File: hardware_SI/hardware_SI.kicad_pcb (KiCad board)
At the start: 2 copper layers, 228 x 147.6 mm, 58 parts, among them J1 Barrel_Jack_Switch, J2 Conn_01x07_Female, J3 USB_B_Micro, Q1 SI2323DS-T1, Q2 SI2323DS-T1, SW1 SW_SPDT, U1 OMEGA2+, U2 LTC4085EDEPBF, U3 TPS61200DRC, U4 LD1117S33TR_SOT223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

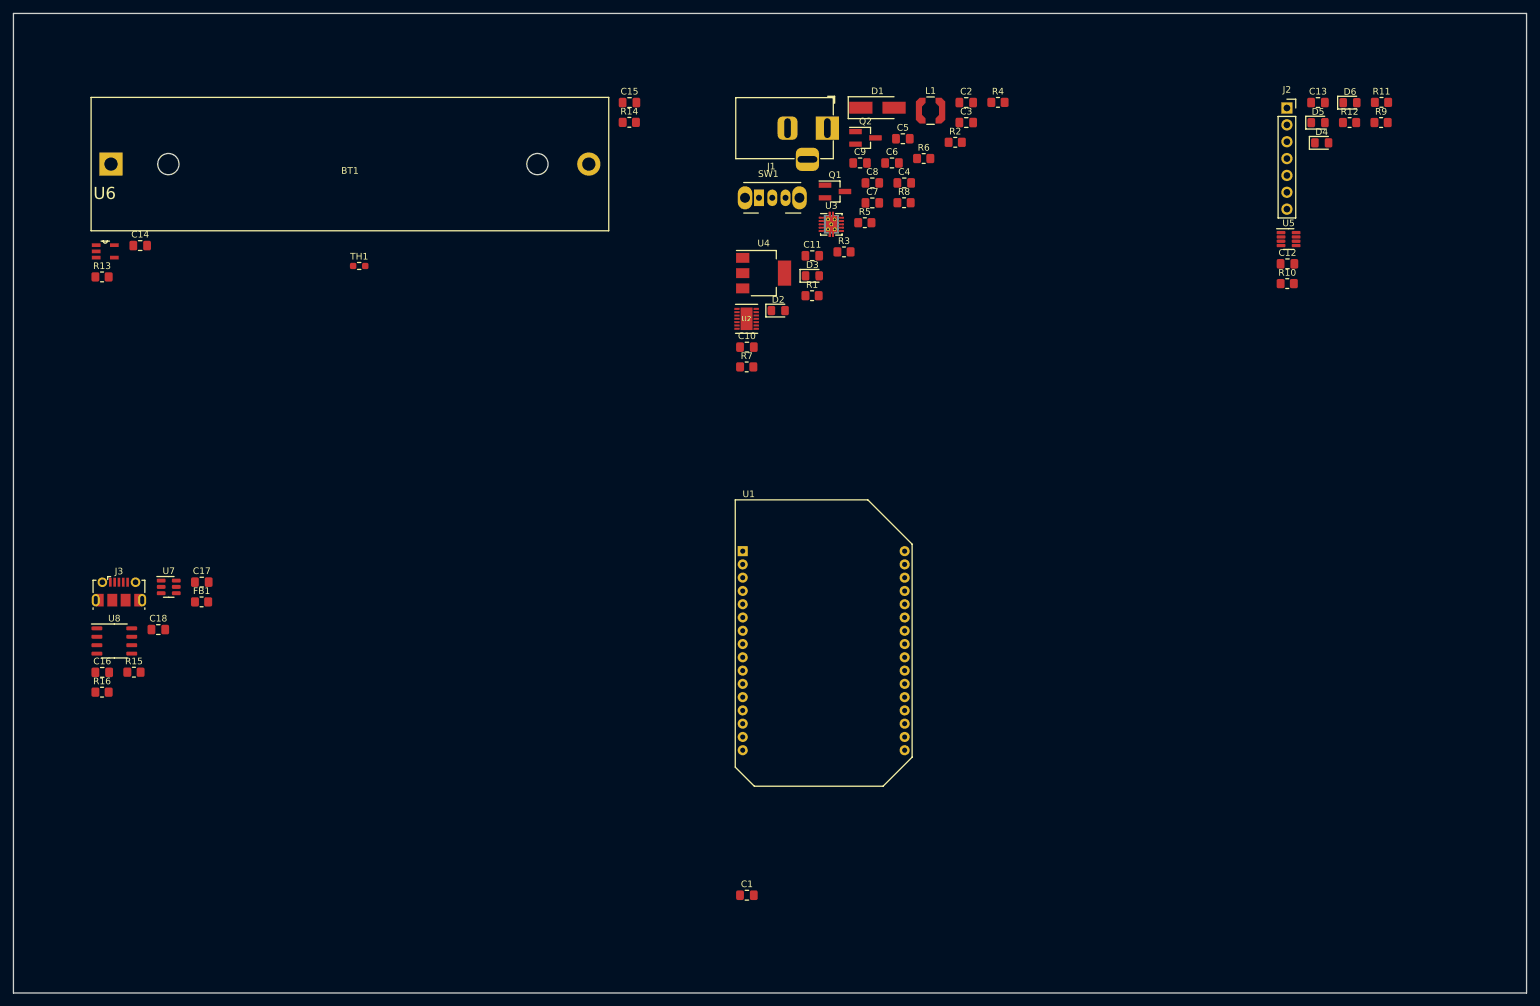
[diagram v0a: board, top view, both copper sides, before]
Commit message: Rutas de PCB
- Se realiza la PCB y se asignan sus respectivas rutas.
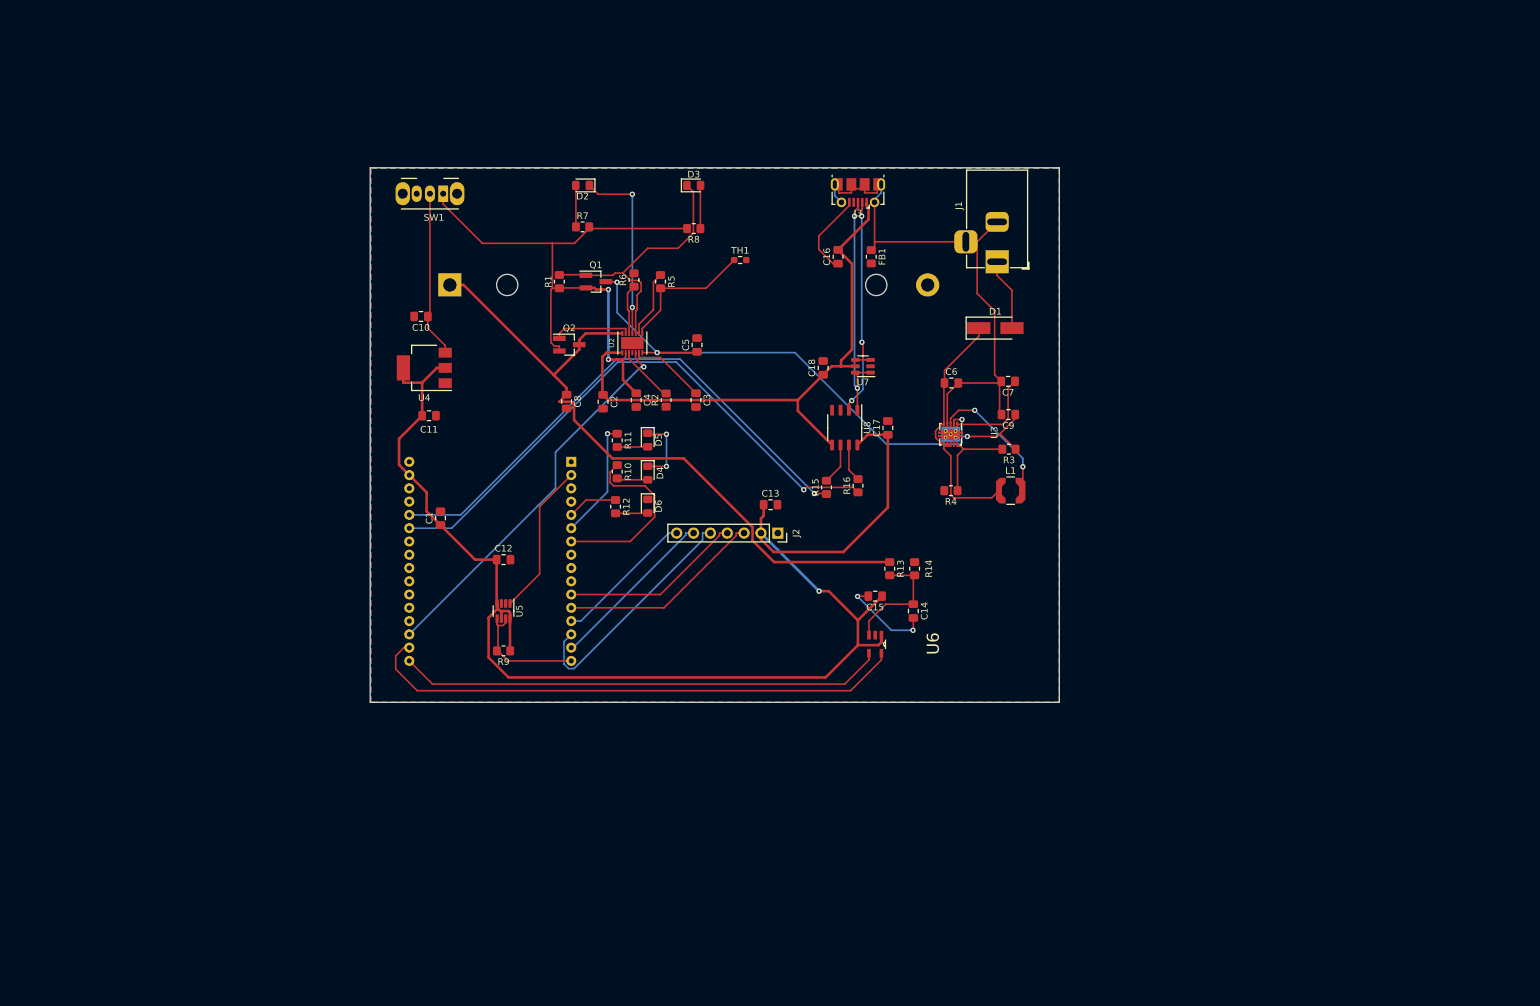
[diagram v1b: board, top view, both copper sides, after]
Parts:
- BT1, U1: moved to B.Cu
- moved R9 154.3 mm to (121.2, 120.2), turned to 180 degrees
- moved U5 130.9 mm to (121.2, 114.2), turned to -90 degrees
- moved U6 130.2 mm to (177.2, 119.2), turned to -90 degrees
- moved C14 128.9 mm to (183.0, 114.2), turned to -90 degrees
- moved C16 127.3 mm to (171.7, 60.9), turned to 90 degrees
- moved J3 126.6 mm to (174.7, 51.2), turned to 180 degrees
- moved R13 126.6 mm to (179.4, 107.9), turned to -90 degrees
- moved C12 126.2 mm to (121.2, 106.5)
- moved R11 125.9 mm to (138.4, 88.5), turned to -90 degrees
- moved R12 124.8 mm to (138.1, 98.5), turned to -90 degrees
- moved D6 122.0 mm to (143.0, 98.5), turned to -90 degrees
- moved R16 118.1 mm to (174.7, 95.4), turned to 90 degrees
- moved U8 114.7 mm to (172.7, 86.6), turned to -90 degrees
- moved FB1 113.5 mm to (176.7, 60.9), turned to -90 degrees
- moved D4 113.1 mm to (143.0, 93.5), turned to -90 degrees
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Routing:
- net +3V3: track 0.00 -> 209.1 mm, vias 0 -> 1
- net +BATT: track 0.00 -> 102.7 mm
- net +5VP: track 0.00 -> 93.4 mm, vias 0 -> 4
- net +5VL: track 0.00 -> 87.6 mm, vias 0 -> 2
- net +5VA: track 0.00 -> 86.7 mm
- net /TX0: track 0.00 -> 86.4 mm, vias 0 -> 1
- net GNDPWR: track 0.00 -> 86.3 mm
- net /SCL: track 0.00 -> 82.0 mm
- net /RX0: track 0.00 -> 81.0 mm, vias 0 -> 1
- net /SDA: track 0.00 -> 73.2 mm
- net /IO19: track 0.00 -> 57.9 mm, vias 0 -> 1
- net /sistema_alimentacion/*ACPR: track 0.00 -> 41.8 mm
- net Net-(C6-Pad1): track 0.00 -> 38.9 mm
- net GND: track 0.00 -> 38.5 mm, vias 0 -> 4
- net Net-(J3-Pad2): track 0.00 -> 37.3 mm, vias 0 -> 3
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- added copper zone on B.Cu, net GND
- added copper zone on F.Cu, net GND
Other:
- board size 228 x 147.6 mm -> 103.8 x 80.5 mm

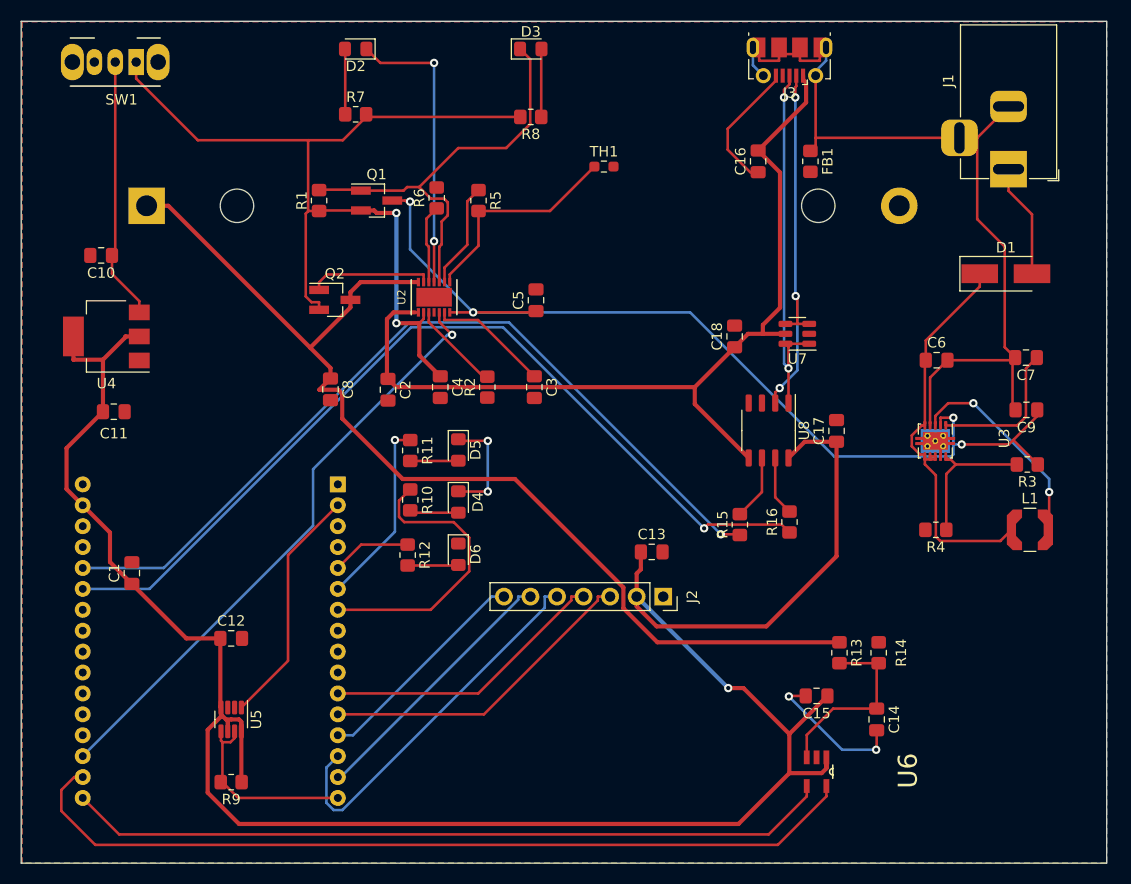
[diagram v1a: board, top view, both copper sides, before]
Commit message: Cambio en alimentación y zona GNDPWR
- Debido a los tiempos de entrega del LTC4085, se cambia el sistema de alimentación, agregando un selector automático de fuente y un integrado de manejo de batería.
- En consecuencia de lo anterior, se usa un LDO con menor voltaje de dropout.
- Se cambia el convertidor DC-DC debido a su alto precio.
- En cuanto a PCB, se completa el circuito del convertidor DC-DC y la zona de GNPWR.
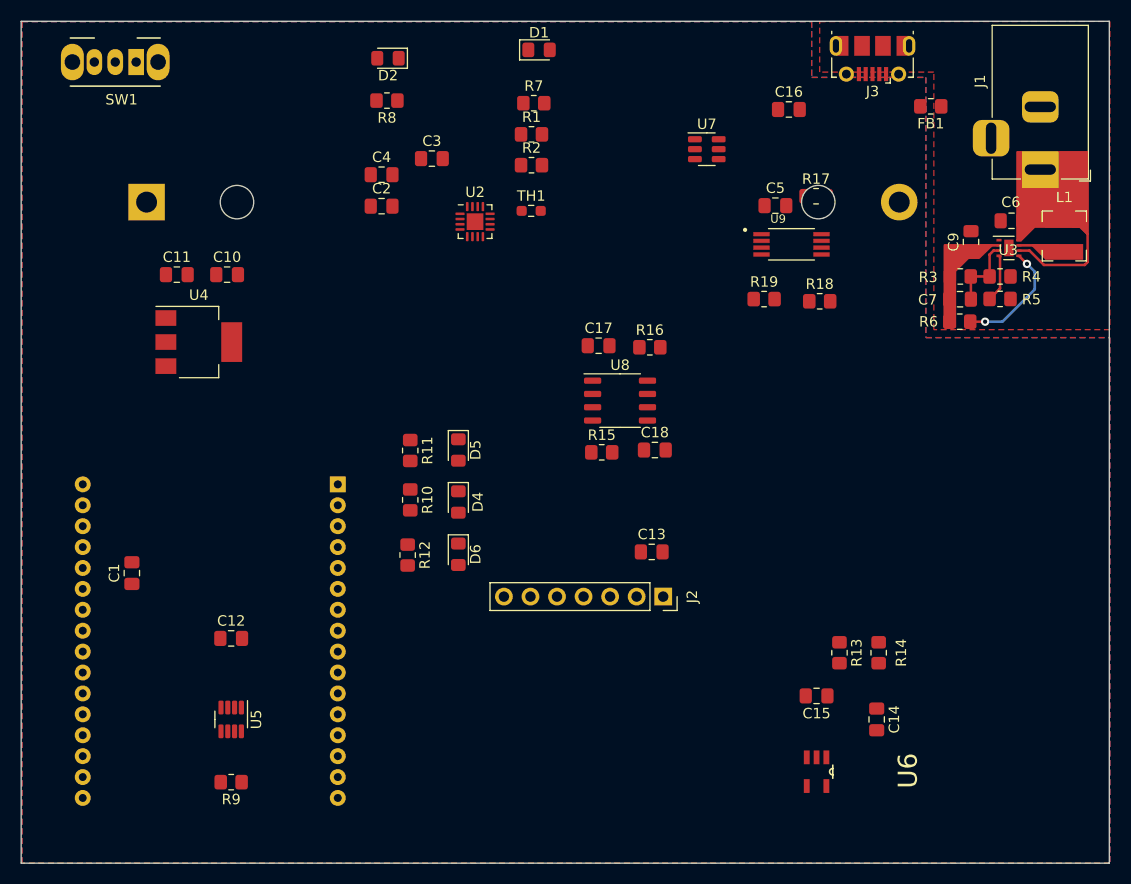
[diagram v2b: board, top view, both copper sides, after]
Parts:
- removed C8: 100n, Capacitor_SMD:C_0805_2012Metric_Pad1.18x1.45mm_HandSolder
- removed D3: WALL_LED, LED_SMD:LED_0805_2012Metric_Pad1.15x1.40mm_HandSolder
- removed Q1, Q2: SI2323DS-T1, Package_TO_SOT_SMD:SOT-23_Handsoldering
- added R17: 10k, Resistor_SMD:R_0805_2012Metric_Pad1.20x1.40mm_HandSolder, F.Cu at (177.2, 64.2)
- added R18: 2.2k, Resistor_SMD:R_0805_2012Metric_Pad1.20x1.40mm_HandSolder, F.Cu at (177.6, 74.2)
- added R19: 400, Resistor_SMD:R_0805_2012Metric_Pad1.20x1.40mm_HandSolder, F.Cu at (172.2, 74.0)
- added U9: TPS2111APWR, TPS2111APWR:SOP65P640X120-8N, F.Cu at (174.8, 68.8)
- C10: value 100n -> 1uF
- C11: value 10u -> 4.7uF
- C2: value 4.7uF -> 1uF
- C3: value 0.1uF -> 4.7uF
- C7: value 100n -> 100pF
- C9: value 10uF -> 22uF
- D1: value 1N4007 -> PGOOD_LED; footprint Diode_SMD:D_SMA_Handsoldering -> LED_SMD:LED_0805_2012Metric_Pad1.15x1.40mm_HandSolder
- L1: value 2.2uH -> 1uH; footprint Inductor_SMD:L_Coilcraft_LPS4018 -> Inductor_SMD:L_Bourns-SRN4018
- R1: value 1k -> 1.5k
- R2: value 2.1k -> 1.5k
- R3: value 1.5M -> 768k
- R4: value 180k -> 243k
- R6: value 10k -> 1M
- R7, R8: value 510 -> 1.5k
- U2: value LTC4085EDEPBF -> BQ24072RGT; footprint LTC4085EDEPBF:DFN-14_DE -> Package_DFN_QFN:VQFN-16-1EP_3x3mm_P0.5mm_EP1.6x1.6mm
- U3: value TPS61200DRC -> TPS61252DSG; footprint Package_SON:Texas_S-PVSON-N10_ThermalVias -> Package_SON:WSON-8-1EP_2x2mm_P0.5mm_EP0.9x1.6mm
- U4: value LD1117S33TR_SOT223 -> LDL1117S33R
- moved R6 51.4 mm to (190.9, 76.2), turned to 180 degrees
- moved R5 50.8 mm to (194.8, 74.0), turned to 0 degrees
- moved D1 49.5 mm to (150.7, 50.2)
- moved L1 28.3 mm to (200.9, 68.0), turned to -90 degrees
- moved R4 25.0 mm to (194.8, 71.9), turned to 0 degrees
- moved C5 24.6 mm to (173.3, 65.1), turned to 0 degrees
- moved C17 24.2 mm to (156.4, 78.5), turned to 0 degrees
- moved C3 24.0 mm to (140.4, 60.6), turned to 0 degrees
- moved R2 21.6 mm to (150.0, 61.2), turned to 0 degrees
- moved R16 21.4 mm to (161.3, 78.7), turned to 0 degrees
- moved R1 21.3 mm to (150.0, 58.3), turned to 0 degrees
- moved C4 21.1 mm to (135.6, 62.1), turned to 0 degrees
- moved U3 19.8 mm to (195.7, 69.2), turned to 0 degrees
- moved U7 19.7 mm to (166.8, 59.7), turned to 0 degrees
- moved R3 19.1 mm to (191.0, 71.9), turned to 0 degrees
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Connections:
- C2 pad 1: +5VA -> GND
- C2 pad 2: GND -> +5VL
- C3 pad 1: Net-(C3-Pad1) -> VCC
- C4 pad 1: +5VL -> +BATT
- C5 pad 1: +5VP -> +5VL
- C6 pad 1: Net-(C6-Pad1) -> Net-(J1-Pad1)
- C7 pad 1: Net-(C7-Pad1) -> +5VP
- C7 pad 2: GNDPWR -> Net-(C7-Pad2)
- D1 pad 1: Net-(C6-Pad1) -> Net-(D1-Pad1)
- J1 pad 1: Net-(D1-Pad2) -> Net-(J1-Pad1)
- L1 pad 1: Net-(C6-Pad1) -> Net-(J1-Pad1)
- R1 pad 1: +5VL -> GND
- R1 pad 2: /sistema_alimentacion/*ACPR -> Net-(R1-Pad2)
- R3 pad 2: Net-(R3-Pad2) -> Net-(C7-Pad2)
- R4 pad 1: Net-(R3-Pad2) -> Net-(C7-Pad2)
- R4 pad 2: GND -> GNDPWR
- R5 pad 2: Net-(R5-Pad2) -> GNDPWR
- R6 pad 2: GND -> +5VP
- R7 pad 1: Net-(D2-Pad2) -> Net-(D1-Pad2)
- R7 pad 2: +5VL -> VCC
- R8 pad 1: Net-(D3-Pad2) -> Net-(D2-Pad2)
- R8 pad 2: +5VL -> VCC
- SW1 pad 1: +5VL -> VCC
- TH1 pad 1: Net-(R5-Pad2) -> Net-(TH1-Pad1)
- U2 pad 1: +5VA -> Net-(TH1-Pad1)
- U2 pad 10: /sistema_alimentacion/*ACPR -> VCC
- U2 pad 11: Net-(D2-Pad1) -> VCC
- U2 pad 12: Net-(R6-Pad1) -> Net-(R1-Pad2)
- U2 pad 13: Net-(Q2-Pad1) -> +5VL
- U2 pad 14: +BATT -> unconnected-(U2-Pad14)
- U2 pad 2: +5VL -> +BATT
- U2 pad 3: Net-(R2-Pad2) -> +BATT
- U2 pad 4: /IO18 -> GND
- U2 pad 5: /IO19 -> VCC
- U2 pad 6: Net-(C3-Pad1) -> GND
- U2 pad 7: +5VP -> Net-(D1-Pad1)
- U2 pad 8: Net-(R5-Pad2) -> GND
- U2 pad 9: Net-(R5-Pad1) -> Net-(D2-Pad1)
- U3 pad 1: Net-(C7-Pad1) -> GNDPWR
- U3 pad 3: Net-(L1-Pad2) -> Net-(C7-Pad2)
- U3 pad 4: GNDPWR -> Net-(R5-Pad1)
- U3 pad 5: Net-(C6-Pad1) -> Net-(R6-Pad1)
- U3 pad 6: Net-(C6-Pad1) -> Net-(J1-Pad1)
- U3 pad 7: Net-(C6-Pad1) -> Net-(L1-Pad2)
- U3 pad 8: Net-(C6-Pad1) -> Net-(J1-Pad1)
- U3 pad 9: GND -> GNDPWR
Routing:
- net +3V3: track 209.1 -> 0.00 mm, vias 1 -> 0
- net +BATT: track 102.7 -> 0.00 mm
- net +5VL: track 87.6 -> 0.00 mm, vias 2 -> 0
- net +5VA: track 86.7 -> 0.00 mm
- net /TX0: track 86.4 -> 0.00 mm, vias 1 -> 0
- net GNDPWR: track 86.3 -> 0.00 mm
- net +5VP: track 93.4 -> 10.4 mm, vias 4 -> 0
- net /SCL: track 82.0 -> 0.00 mm
- net /RX0: track 81.0 -> 0.00 mm, vias 1 -> 0
- net /SDA: track 73.2 -> 0.00 mm
- net /IO19: track 57.9 -> 0.00 mm, vias 1 -> 0
- net /sistema_alimentacion/*ACPR: track 41.8 -> 0.00 mm
- net Net-(C6-Pad1): track 38.9 -> 0.00 mm
- net GND: track 38.5 -> 0.00 mm, vias 4 -> 0
- net Net-(J3-Pad2): track 37.3 -> 0.00 mm, vias 3 -> 0
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- added copper zone on F.Cu, net GNDPWR
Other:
- board size 103.8 x 80.5 mm -> 104.1 x 80.5 mm

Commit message: PCB corregido
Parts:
- added ?: , , F.Cu at (128.8, 50.2)
- added ?: , , F.Cu at (203.8, 122.0)
- added ?: , , F.Cu at (128.8, 121.8)
- moved BT1 90.2 mm to (201.9, 80.7), turned to 180 degrees
- moved C1 61.5 mm to (170.5, 118.6), turned to 180 degrees
- moved R9 51.0 mm to (170.6, 107.2), turned to 0 degrees
- moved C12 49.8 mm to (170.5, 113.8), turned to 180 degrees
- moved U5 49.5 mm to (170.6, 110.5), turned to 90 degrees
- moved U1 38.4 mm to (169.5, 96.6), turned to -90 degrees
- moved SW1 38.3 mm to (150.4, 50.5)
- moved C4 34.5 mm to (170.0, 65.5), turned to 90 degrees
- moved C18 32.7 mm to (169.3, 56.6), turned to -90 degrees
- moved C11 31.2 mm to (147.0, 67.8), turned to 90 degrees
- moved C2 30.0 mm to (165.1, 70.9), turned to 90 degrees
- moved R15 28.5 mm to (158.6, 60.3)
- moved U4 27.1 mm to (142.2, 65.6), turned to -90 degrees
- moved U8 27.0 mm to (165.5, 57.6), turned to 90 degrees
- moved R8 26.9 mm to (162.9, 52.3)
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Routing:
- net +3V3: track 0.00 -> 212.4 mm, vias 0 -> 1
- net /TX0: track 0.00 -> 79.5 mm, vias 0 -> 2
- net /RX0: track 0.00 -> 78.7 mm
- net +BATT: track 0.00 -> 65.5 mm
- net VCC: track 0.00 -> 54.6 mm, vias 0 -> 2
- net /CS1: track 0.00 -> 40.1 mm
- net /D/C: track 0.00 -> 40.0 mm
- net /RST_W: track 0.00 -> 38.6 mm
- net /RST_OLED: track 0.00 -> 35.8 mm
- net +5VA: track 0.00 -> 33.6 mm
- net /IO15: track 0.00 -> 31.2 mm, vias 0 -> 1
- net /IO16: track 0.00 -> 27.3 mm, vias 0 -> 1
- net /MOSI: track 0.00 -> 26.8 mm
- net /IO17: track 0.00 -> 23.7 mm, vias 0 -> 1
- net Net-(J3-Pad3): track 0.00 -> 23.4 mm, vias 0 -> 2
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- added copper zone on F.Cu, net +5VP
- added copper zone on F.Cu, net Net-(C6-Pad1)
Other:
- board size 104.1 x 80.5 mm -> 80.2 x 76.9 mm

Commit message: Archivos de fabricación y cambios menores
- Se generan los archivos de fabricación.
- Se cambian algunas resistencias por valores más comerciales.
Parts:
- R19: value 400 -> 470
- R3: value 768k -> 750k; footprint Resistor_SMD:R_0805_2012Metric_Pad1.20x1.40mm_HandSolder -> Resistor_SMD:R_0603_1608Metric_Pad0.98x0.95mm_HandSolder
- R4: value 243k -> 240k; footprint Resistor_SMD:R_0805_2012Metric_Pad1.20x1.40mm_HandSolder -> Resistor_SMD:R_0603_1608Metric_Pad0.98x0.95mm_HandSolder
- moved R3 21.3 mm to (177.8, 88.7)
- moved ? 21.2 mm to (190.8, 138.8)
- moved ? 21.2 mm to (115.8, 138.6)
- moved C1 21.2 mm to (157.5, 135.4)
- moved C14 21.2 mm to (186.4, 125.5)
- moved C15 21.2 mm to (182.8, 125.5)
- moved C4 21.2 mm to (157.0, 82.3)
- moved J2 21.2 mm to (162.3, 109.9)
- moved R10 21.2 mm to (146.7, 95.4)
- moved R14 21.2 mm to (189.1, 125.5)
- moved R2 21.2 mm to (155.9, 87.6)
- moved TH1 21.2 mm to (153.9, 97.9)
- moved U1 21.2 mm to (156.5, 113.4)
- moved U2 21.2 mm to (153.4, 83.3)
- moved U4 21.2 mm to (129.2, 82.4)
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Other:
- board size 80.2 x 76.9 mm -> 80.2 x 77 mm
